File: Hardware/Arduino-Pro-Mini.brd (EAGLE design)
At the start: 17.8 x 33 mm, 29 parts, among them Q1 8/16/20MHz, U1 ATMEGA328, U2 MIC5205

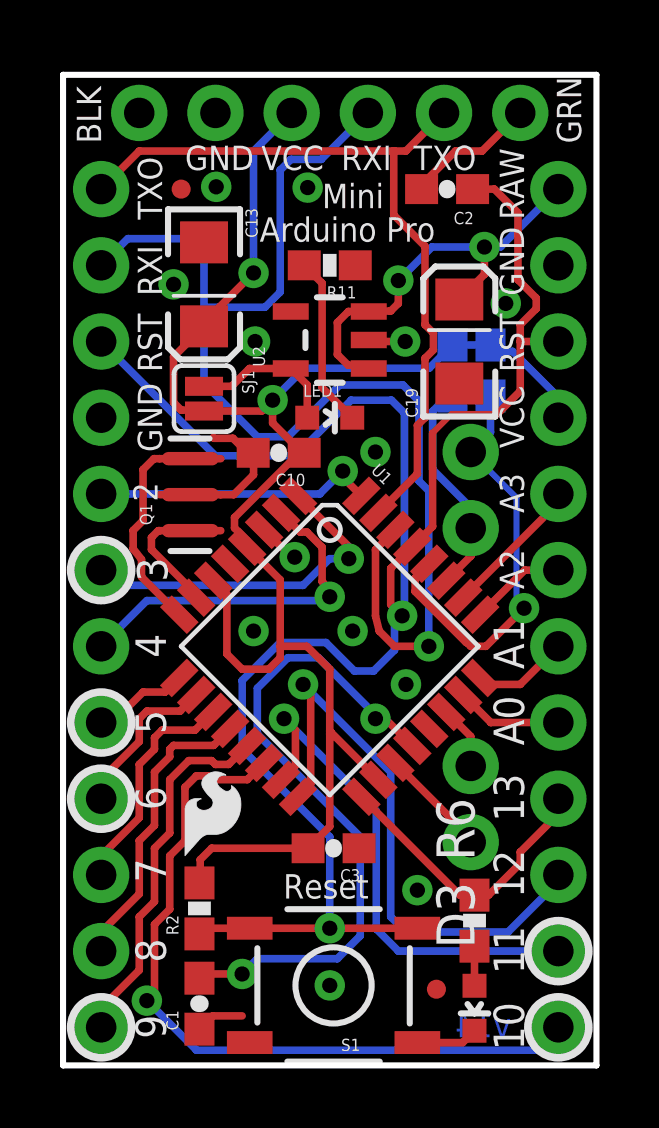
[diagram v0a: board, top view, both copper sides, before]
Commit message: v14 ready for protos
changed led footprint to cloaser to true 0603
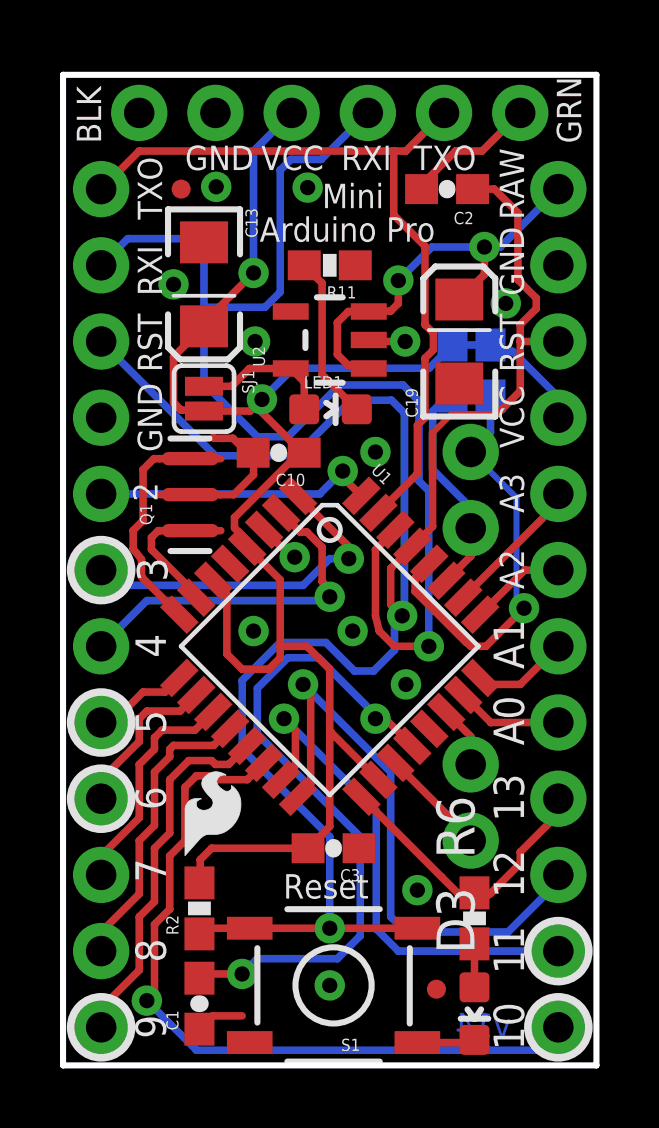
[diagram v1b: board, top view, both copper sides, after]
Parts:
- D3, LED1: device SparkFun:LED-0603 -> Testing:0603-LED-ALT1
- moved LED1 0.28 mm to (8.92, 21.9)
- moved D3 0.18 mm to (13.7, 1.73)
- moved R6 0.08 mm to (13.7, 4.90)
- moved JP3 0.05 mm to (13.6, 7.49)
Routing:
- net GND: track 9.92 -> 9.36 mm
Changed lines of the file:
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@@
 <attribute name="VALUE" x="7.5565" y="26.797" size="0.4064" layer="27" rot="R180"/>
 </element>
-<element name="LED1" library="SparkFun" package="LED-0603" value="Red" x="8.89" y="21.59" smashed="yes" rot="R270">
-<attribute name="NAME" x="8.001" y="22.2885" size="0.4064" layer="25"/>
-<attribute name="VALUE" x="10.414" y="21.3995" size="0.4064" layer="27"/>
+<element name="LED1" library="Testing" package="0603-LED-ALT1" value="Red" x="8.9154" y="21.8694" smashed="yes" rot="R270">
+<attribute name="NAME" x="8.0264" y="22.5679" size="0.4064" layer="25"/>
+<attribute name="VALUE" x="10.4394" y="21.6789" size="0.4064" layer="27"/>
 </element>
 <element name="R2" library="SparkFun" package="0603-RES" value="10K" x="4.5466" y="5.2324" smashed="yes" rot="R90">
@@
 <attribute name="VALUE" x="5.5372" y="1.2827" size="0.4064" layer="27" rot="R90"/>
 </element>
-<element name="R6" library="SparkFun" package="0603-RES" value="330" x="13.716" y="4.826" smashed="yes" rot="R270">
-<attribute name="NAME" x="13.716" y="6.826" size="1.27" layer="25" rot="R90"/>
-<attribute name="VALUE" x="13.081" y="4.4836" size="0.4064" layer="27" rot="R90"/>
-</element>
-<element name="D3" library="SparkFun" package="LED-0603" value="Green" x="13.716" y="1.905" smashed="yes" rot="R180">
-<attribute name="NAME" x="13.716" y="3.905" size="1.27" layer="25" rot="R90"/>
-<attribute name="VALUE" x="13.0556" y="1.1562" size="0.4064" layer="27" rot="R90"/>
+<element name="R6" library="SparkFun" package="0603-RES" value="330" x="13.716" y="4.9022" smashed="yes" rot="R270">
+<attribute name="NAME" x="13.716" y="6.9022" size="1.27" layer="25" rot="R90"/>
+<attribute name="VALUE" x="13.081" y="4.5598" size="0.4064" layer="27" rot="R90"/>
+</element>
+<element name="D3" library="Testing" package="0603-LED-ALT1" value="Green" x="13.716" y="1.7272" smashed="yes" rot="R180">
+<attribute name="NAME" x="13.716" y="3.7272" size="1.27" layer="25" rot="R90"/>
+<attribute name="VALUE" x="13.0556" y="0.9784" size="0.4064" layer="27" rot="R90"/>
 </element>
 <element name="U$11" library="SparkFun" package="SFE-NEW-WEBLOGO" value="LOGO-SFENEW" x="7.112" y="7.239" rot="MR90"/>
@@
 <element name="SJ1" library="SparkFun-Passives" package="SJ_2S" value="" x="4.699" y="22.225" rot="R270"/>
 <element name="S1" library="Testing" package="TACTILE-SWITCH-SMD-ALT01" value="Reset" x="9.017" y="2.667" rot="R180"/>
-<element name="JP3" library="SparkFun" package="1X02" value="" x="13.589" y="7.4422" rot="MR90"/>
+<element name="JP3" library="SparkFun" package="1X02" value="" x="13.589" y="7.493" rot="MR90"/>
 <element name="Q1" library="Testing" package="RESONATOR-SMD-1:1" value="8/16/20MHz" x="4.2418" y="19.0246" rot="R90"/>
 </elements>
@@
 <contactref element="S1" pad="2"/>
 <via x="11.811" y="5.842" extent="1-16" drill="0.508"/>
-<wire x1="13.716" y1="1.155" x2="13.323" y2="0.762" width="0.254" layer="1"/>
 <wire x1="13.323" y1="0.762" x2="11.811" y2="0.762" width="0.254" layer="1"/>
 <contactref element="Q1" pad="2"/>
@@
 <wire x1="15.24" y1="7.112" x2="16.51" y2="8.382" width="0.254" layer="1"/>
 <wire x1="15.24" y1="6.731" x2="15.24" y2="7.112" width="0.254" layer="1"/>
-<wire x1="14.185" y1="5.676" x2="15.24" y2="6.731" width="0.254" layer="1"/>
-<wire x1="9.945425" y1="8.954771875" x2="13.224196875" y2="5.676" width="0.254" layer="1"/>
-<wire x1="13.224196875" y1="5.676" x2="13.716" y2="5.676" width="0.254" layer="1"/>
-<wire x1="14.185" y1="5.676" x2="13.716" y2="5.676" width="0.254" layer="1"/>
+<wire x1="14.185" y1="5.676" x2="14.2612" y2="5.7522" width="0.254" layer="1"/>
+<wire x1="9.945425" y1="8.954771875" x2="12.6251" y2="6.275096875" width="0.254" layer="1"/>
+<wire x1="13.147996875" y1="5.7522" x2="13.224196875" y2="5.676" width="0.254" layer="1"/>
+<wire x1="13.716" y1="5.7522" x2="14.2612" y2="5.7522" width="0.254" layer="1"/>
+<wire x1="14.2612" y1="5.7522" x2="15.24" y2="6.731" width="0.254" layer="1"/>
+<wire x1="13.716" y1="5.7522" x2="13.147996875" y2="5.7522" width="0.254" layer="1"/>
+<wire x1="13.147996875" y1="5.7522" x2="12.6251" y2="6.275096875" width="0.254" layer="1"/>
 </signal>
 <signal name="MISO">
@@
 <contactref element="R6" pad="2"/>
 <contactref element="D3" pad="A"/>
-<wire x1="13.716" y1="2.655" x2="13.716" y2="3.976" width="0.254" layer="1"/>
+<wire x1="13.716" y1="2.6042" x2="13.716" y2="4.0522" width="0.254" layer="1"/>
 </signal>
 <signal name="TXO">
@@
 <wire x1="16.51" y1="22.2758" x2="16.51" y2="21.59" width="0.254" layer="16"/>
 <wire x1="14.986" y1="23.7998" x2="16.51" y2="22.2758" width="0.254" layer="16"/>
-<wire x1="8.0518" y1="23.241" x2="12.2056" y2="23.241" width="0.254" layer="16"/>
-<wire x1="6.985" y1="22.1742" x2="8.0518" y2="23.241" width="0.254" layer="16"/>
+<wire x1="7.6708" y1="23.241" x2="12.2056" y2="23.241" width="0.254" layer="16"/>
 <wire x1="12.9794" y1="24.0148" x2="14.2494" y2="24.0148" width="0.254" layer="16"/>
-<via x="6.985" y="22.1742" extent="1-16" drill="0.508"/>
+<via x="6.6294" y="22.1996" extent="1-16" drill="0.508"/>
 <wire x1="8.89" y1="11.0491" x2="8.89" y2="7.962" width="0.254" layer="1"/>
 <wire x1="8.89" y1="7.962" x2="8.167" y2="7.239" width="0.254" layer="1"/>
@@
 <wire x1="6.35" y1="26.416" x2="4.699" y2="24.765" width="0.254" layer="1"/>
 <wire x1="4.699" y1="24.765" x2="4.699" y2="24.635" width="0.254" layer="1"/>
-<wire x1="6.7818" y1="21.971" x2="6.985" y2="22.1742" width="0.254" layer="1"/>
 <wire x1="3.683" y1="22.098" x2="3.937" y2="21.844" width="0.254" layer="1"/>
 <wire x1="3.937" y1="21.844" x2="4.6681" y2="21.844" width="0.254" layer="1"/>
 <wire x1="4.6681" y1="21.844" x2="4.699" y2="21.8131" width="0.254" layer="1"/>
-<wire x1="4.699" y1="21.8131" x2="6.6239" y2="21.8131" width="0.254" layer="1"/>
-<wire x1="6.6239" y1="21.8131" x2="6.985" y2="22.1742" width="0.254" layer="1"/>
 <wire x1="6.35" y1="30.48" x2="7.62" y2="31.75" width="0.254" layer="16"/>
 <wire x1="6.137515625" y1="17.313484375" x2="6.137515625" y2="17.28816875" width="0.254" layer="1"/>
@@
 <wire x1="6.137515625" y1="17.491284375" x2="6.137515625" y2="17.28816875" width="0.254" layer="1"/>
 <wire x1="7.874" y1="20.4216" x2="8.0382" y2="20.4216" width="0.254" layer="1"/>
-<wire x1="6.985" y1="22.1742" x2="6.985" y2="21.4122" width="0.254" layer="1"/>
-<wire x1="6.985" y1="21.4122" x2="7.9756" y2="20.4216" width="0.254" layer="1"/>
+<wire x1="6.6294" y1="21.7678" x2="7.9756" y2="20.4216" width="0.254" layer="1"/>
 <wire x1="7.9756" y1="20.4216" x2="8.0382" y2="20.4216" width="0.254" layer="1"/>
+<wire x1="7.6708" y1="23.241" x2="6.6294" y2="22.1996" width="0.254" layer="16"/>
+<wire x1="6.6294" y1="21.7678" x2="6.6294" y2="22.1996" width="0.254" layer="1"/>
+<wire x1="4.699" y1="21.8131" x2="6.2429" y2="21.8131" width="0.254" layer="1"/>
+<wire x1="6.2429" y1="21.8131" x2="6.6294" y2="22.1996" width="0.254" layer="1"/>
 </signal>
 <signal name="RAW" class="1">
@@
 <contactref element="JP3" pad="1"/>
 <wire x1="11.076796875" y1="10.08614375" x2="13.589" y2="7.573940625" width="0.254" layer="1"/>
-<wire x1="13.589" y1="7.573940625" x2="13.589" y2="7.4422" width="0.254" layer="1"/>
+<wire x1="13.589" y1="7.573940625" x2="13.589" y2="7.493" width="0.254" layer="1"/>
 </signal>
 <signal name="A7">
@@
 <wire x1="12.773853125" y1="11.783146875" x2="12.773853125" y2="11.7832" width="0.254" layer="1"/>
 <contactref element="JP3" pad="2"/>
-<wire x1="13.589" y1="10.968" x2="13.589" y2="9.9822" width="0.254" layer="1"/>
+<wire x1="13.589" y1="10.968" x2="13.589" y2="10.033" width="0.254" layer="1"/>
 </signal>
 <signal name="N$3">
@@
 <contactref element="SJ1" pad="1"/>
 <contactref element="LED1" pad="A"/>
-<wire x1="7.5899" y1="23.2308" x2="8.14" y2="22.6807" width="0.254" layer="1"/>
-<wire x1="8.14" y1="22.6807" x2="8.14" y2="21.59" width="0.254" layer="1"/>
 <wire x1="7.5899" y1="23.2308" x2="6.2128" y2="23.2308" width="0.254" layer="1"/>
 <wire x1="6.2128" y1="23.2308" x2="5.6189" y2="22.6369" width="0.254" layer="1"/>
 <wire x1="4.699" y1="22.6369" x2="5.6189" y2="22.6369" width="0.254" layer="1"/>
+<wire x1="8.0384" y1="21.8694" x2="8.0384" y2="22.7823" width="0.254" layer="1"/>
+<wire x1="8.0384" y1="22.7823" x2="7.5899" y2="23.2308" width="0.254" layer="1"/>
 </signal>
 <signal name="N$4">
 <contactref element="R11" pad="2"/>
 <contactref element="LED1" pad="C"/>
-<wire x1="8.636" y1="22.594" x2="8.636" y2="26.074" width="0.254" layer="1"/>
-<wire x1="8.636" y1="22.594" x2="9.64" y2="21.59" width="0.254" layer="1"/>
+<wire x1="8.636" y1="23.0258" x2="8.636" y2="26.074" width="0.254" layer="1"/>
 <wire x1="8.636" y1="26.074" x2="8.04" y2="26.67" width="0.254" layer="1"/>
+<wire x1="9.7924" y1="21.8694" x2="8.636" y2="23.0258" width="0.254" layer="1"/>
 </signal>
 </signals>

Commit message: Finished design review and checklist
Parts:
- removed FRAME1: FRAME-LETTER, SparkFun-Aesthetics:CREATIVE_COMMONS
- removed U$1: LOGO-SFESK, SparkFun:SFE-LOGO-FLAME
- removed U$11: LOGO-SFENEW, SparkFun:SFE-NEW-WEBLOGO
- removed U$3: OSHW-LOGOS, SparkFun:OSHW-LOGO-S
- added FRAME2: FRAME-LETTER, SparkFun-Aesthetics:CREATIVE_COMMONS
- JP6, JP7: value (none) -> M12PTH
- Q1: device Testing:RESONATOR-SMD-1:1 -> SparkFun:RESONATOR-SMD-1:1
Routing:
- net GND: track 9.36 -> 10.4 mm
- net N$2: track 3.39 -> 4.41 mm
- net N$1: track 6.30 -> 7.32 mm
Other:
- board text added: "ORDER"
- board text added: "Original Arduino Mini Design by Team Arduino Arduino Pro Mini Design by SparkFun Electronics Revised by Pete Lewis and Marshall Taylor"
- board text added: "PCBS"
- board text added: "THIN"
- board text added: "v15"
- board text removed: "10"
- board text removed: "10MHz"
- board text removed: "11"
- board text removed: "12"
- board text removed: "13"
- board text removed: "16MHz"
- board text removed: "2"
- board text removed: "20MHz"
- board text removed: "3"
- board text removed: "3.3V"
- board text removed: "4"
- board text removed: "5"
- board text removed: "5V"
- board text removed: "6"
- board text removed: "7"
- board text removed: "8"
- board text removed: "8MHz"
- board text removed: "9"
- board text removed: "A0"
- board text removed: "A1"
- board text removed: "A2"
- board text removed: "A3"
- board text removed: "A4"
- board text removed: "A5"
- board text removed: "A6"
- board text removed: "A7"
- board text removed: "Arduino Pro"
- board text removed: "Arduino Pro Mini"
- board text removed: "BLK"
- board text removed: "GND"
- board text removed: "GRN"
- board text removed: "Mini"
- board text removed: "Original Arduino Mini Design by Team Arduino Arduino Pro Mini Design by SparkFun Electronics Revised by Pete Lewis"
- board text removed: "RAW"
- board text removed: "RST"
- board text removed: "RXI"
- board text removed: "Reset"
- board text removed: "TXO"
- board text removed: "VCC"
- board text removed: "v14"
- board text removed: "www.arduino.cc"

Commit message: Fixed schematic issues
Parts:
- Q1: value 8/16/20MHz -> 8/16MHz
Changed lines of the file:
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@@
 <layer number="112" name="tSilk" color="7" fill="1" visible="no" active="yes"/>
 <layer number="113" name="IDFDebug" color="4" fill="1" visible="no" active="yes"/>
-<layer number="114" name="Badge_Outline" color="7" fill="1" visible="yes" active="yes"/>
-<layer number="115" name="ReferenceISLANDS" color="7" fill="1" visible="yes" active="yes"/>
+<layer number="114" name="Badge_Outline" color="7" fill="1" visible="no" active="yes"/>
+<layer number="115" name="ReferenceISLANDS" color="7" fill="1" visible="no" active="yes"/>
 <layer number="116" name="Patch_BOT" color="9" fill="4" visible="no" active="yes"/>
-<layer number="118" name="Rect_Pads" color="7" fill="1" visible="yes" active="yes"/>
+<layer number="118" name="Rect_Pads" color="7" fill="1" visible="no" active="yes"/>
 <layer number="121" name="_tsilk" color="7" fill="1" visible="no" active="yes"/>
 <layer number="122" name="_bsilk" color="7" fill="1" visible="no" active="yes"/>
@@
 </element>
 <element name="JP3" library="SparkFun" package="1X02" value="" x="13.589" y="7.493" rot="MR90"/>
-<element name="Q1" library="SparkFun" package="RESONATOR-SMD-1:1" value="8/16/20MHz" x="4.2418" y="19.0246" rot="R90">
+<element name="Q1" library="SparkFun" package="RESONATOR-SMD-1:1" value="8/16MHz" x="4.2418" y="19.0246" rot="R90">
 <attribute name="PROD_ID" value="XTAL-08900" x="4.2418" y="19.0246" size="1.778" layer="27" rot="R90" display="off"/>
 </element>

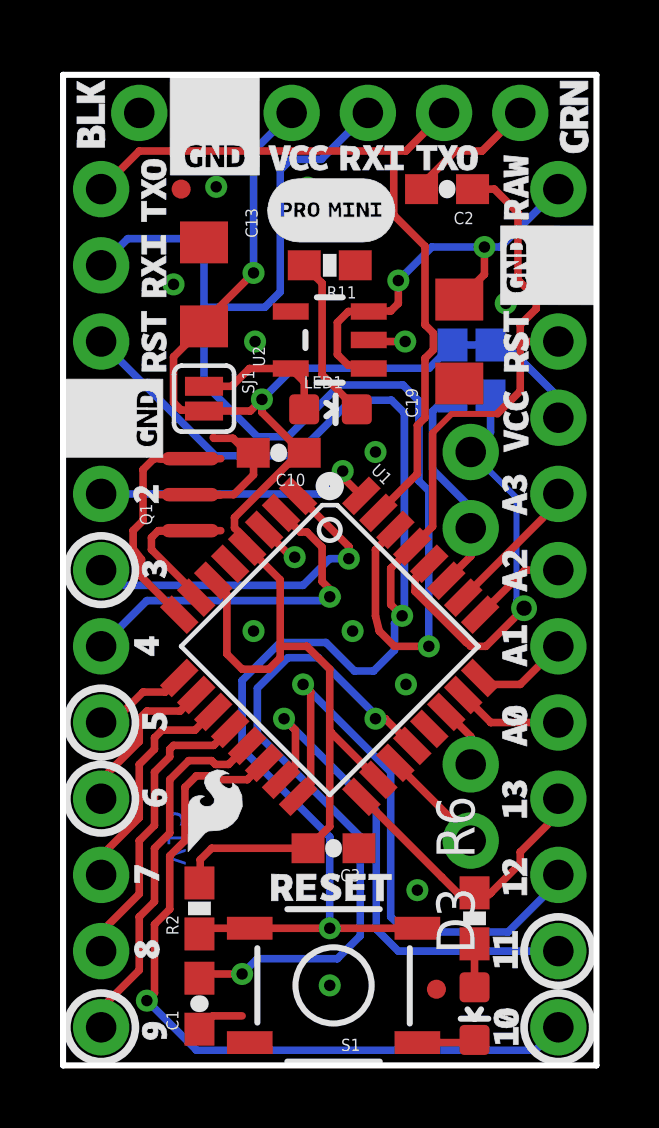
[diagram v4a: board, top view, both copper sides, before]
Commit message: Re-imported silk graphics, moved a couple ground vias, incremented version number to 1.6
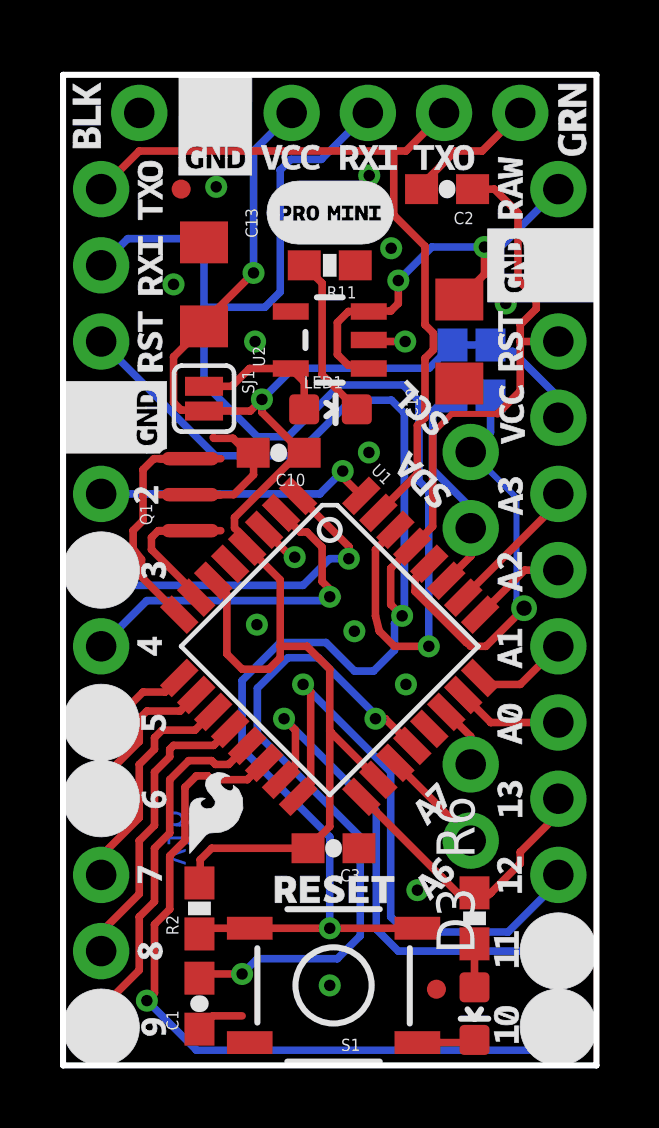
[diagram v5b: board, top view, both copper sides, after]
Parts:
- moved FRAME2 5.08 mm to (-31.8, -17.8)
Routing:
- net GND: vias 13 -> 14
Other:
- board text added: "(168 / 5V Reg / 20MHz no longer used)"
- board text added: "(Add these comments when uploading gerbers.)"
- board text added: "Ordering Instructions:"
- board text added: "Thin PCB: 0.032 inch Blue soldermask: about 0% Red, 39% Green, 59% Blue. (Hex code: #006496)"
- board text added: "v16"
- board text removed: "168 / 5V Reg / 20MHz"
- board text removed: "ORDER"
- board text removed: "PCBS"
- board text removed: "THIN"
- board text removed: "v15"

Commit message: Post review and checklist verification
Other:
- board text added: "Thin PCB: 0.032 inch (0.8 mm) Blue soldermask: Screen color: 0% Red, 39% Green, 59% Blue. (Hex code: #006496) Pantone: 308 C / 315 U"
- board text removed: "(168 / 5V Reg / 20MHz no longer used)"
- board text removed: "168 / 5V Reg / 16MHz"
- board text removed: "168V / 3.3V Reg / 8MHz"
- board text removed: "Mark back accordingly"
- board text removed: "Thin PCB: 0.032 inch Blue soldermask: about 0% Red, 39% Green, 59% Blue. (Hex code: #006496)"
- board text removed: "Valid combinations:"

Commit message: Incremented version numbers
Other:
- board text added: "v20"
- board text removed: "v16"
